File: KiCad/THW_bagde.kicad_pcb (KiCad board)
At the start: 2 copper layers, 84.9 x 84.9 mm, 19 parts, among them J1 USB_B, SW1 SW_Push, SW2 SW_Push, SW3 SW_Push, U1 ATmega32L-8P

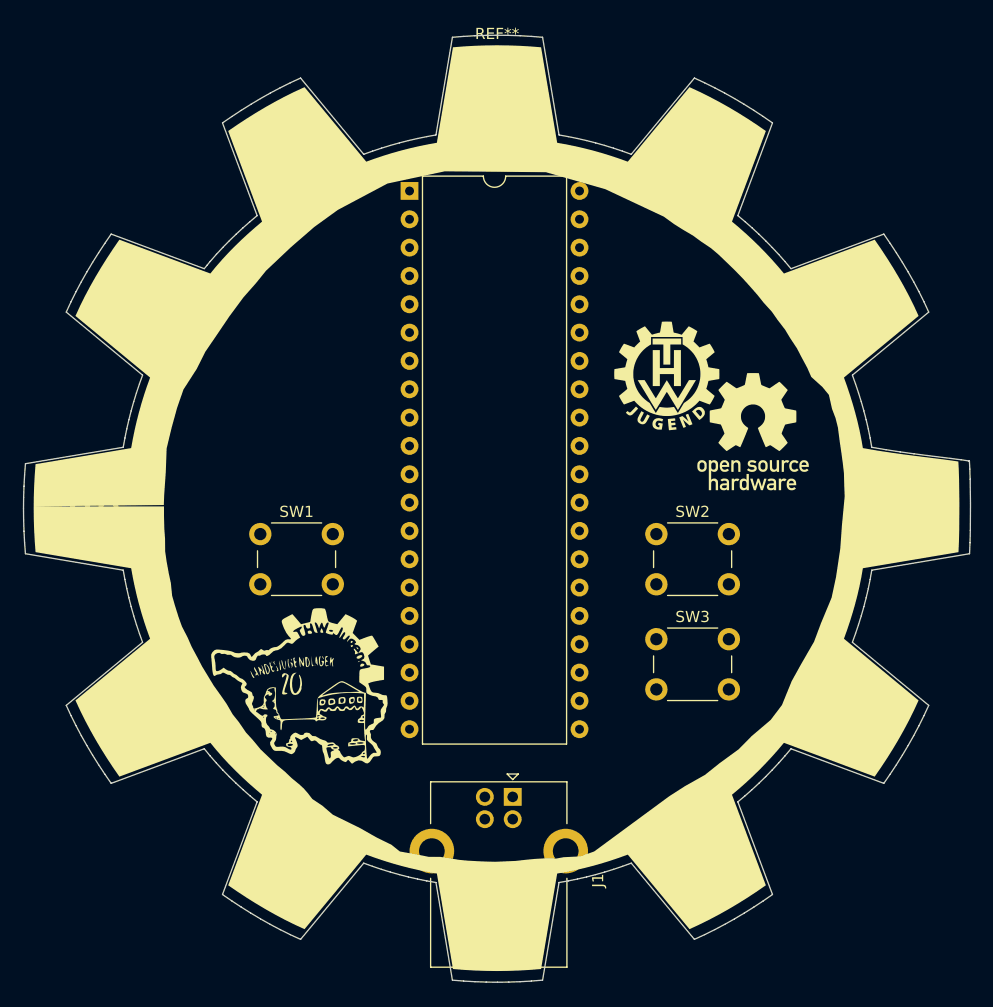
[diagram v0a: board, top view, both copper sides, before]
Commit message: place some parts to see dimension of badge
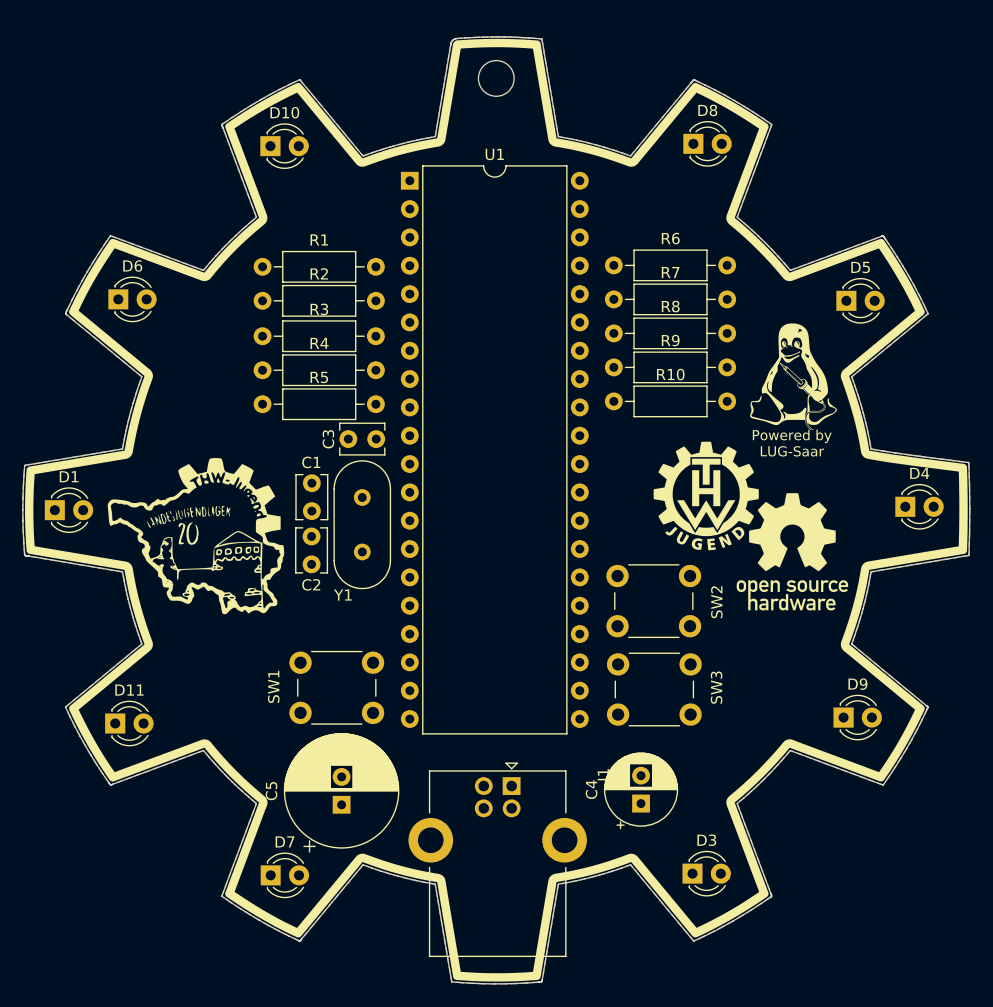
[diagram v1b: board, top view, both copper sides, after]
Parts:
- removed the REF** at (151.6, 53.9)
- added C1: C, Capacitor_THT:C_Disc_D3.8mm_W2.6mm_P2.50mm, F.Cu at (135.0, 92.5)
- added C2: C, Capacitor_THT:C_Disc_D3.8mm_W2.6mm_P2.50mm, F.Cu at (135.0, 97.3)
- added C3: C, Capacitor_THT:C_Disc_D3.8mm_W2.6mm_P2.50mm, F.Cu at (138.2, 86.1)
- added C4: C_Polarized, Capacitor_THT:CP_Radial_D6.3mm_P2.50mm, F.Cu at (164.5, 118.7)
- added C5: C_Polarized, Capacitor_THT:CP_Radial_D10.0mm_P2.50mm, F.Cu at (137.6, 118.8)
- added G***: LOGO, LOGO, F.Cu at (178.2, 78.8)
- added R1: R, Resistor_THT:R_Axial_DIN0207_L6.3mm_D2.5mm_P10.16mm_Horizontal, F.Cu at (130.6, 70.6)
- added R10: R, Resistor_THT:R_Axial_DIN0207_L6.3mm_D2.5mm_P10.16mm_Horizontal, F.Cu at (162.1, 82.7)
- added R2: R, Resistor_THT:R_Axial_DIN0207_L6.3mm_D2.5mm_P10.16mm_Horizontal, F.Cu at (130.6, 73.7)
- added R3: R, Resistor_THT:R_Axial_DIN0207_L6.3mm_D2.5mm_P10.16mm_Horizontal, F.Cu at (130.6, 76.8)
- added R4: R, Resistor_THT:R_Axial_DIN0207_L6.3mm_D2.5mm_P10.16mm_Horizontal, F.Cu at (130.6, 79.9)
- added R5: R, Resistor_THT:R_Axial_DIN0207_L6.3mm_D2.5mm_P10.16mm_Horizontal, F.Cu at (130.6, 82.9)
- added R6: R, Resistor_THT:R_Axial_DIN0207_L6.3mm_D2.5mm_P10.16mm_Horizontal, F.Cu at (162.1, 70.5)
- added R7: R, Resistor_THT:R_Axial_DIN0207_L6.3mm_D2.5mm_P10.16mm_Horizontal, F.Cu at (162.1, 73.5)
- added R8: R, Resistor_THT:R_Axial_DIN0207_L6.3mm_D2.5mm_P10.16mm_Horizontal, F.Cu at (162.1, 76.6)
- added R9: R, Resistor_THT:R_Axial_DIN0207_L6.3mm_D2.5mm_P10.16mm_Horizontal, F.Cu at (162.1, 79.6)
- added REF**: MountingHole_3.2mm_M3_DIN965, MountingHole:MountingHole_3.2mm_M3_DIN965, F.Cu at (151.5, 53.7)
- added Y1: Crystal, Crystal:Crystal_HC49-4H_Vertical, F.Cu at (139.5, 96.2)
- moved G*** 16.3 mm to (124.7, 93.9)
- moved SW1 12.1 mm to (134.0, 106.1)
- moved G*** 11.3 mm to (170.3, 91.2)
- moved G*** 11.3 mm to (178.1, 96.2)
- moved SW2 5.12 mm to (162.4, 98.3)
- moved SW3 4.11 mm to (162.4, 106.3)
- moved D1 2.27 mm to (111.9, 92.4)
- moved D11 1.71 mm to (117.3, 111.6)
- moved D3 1.60 mm to (169.1, 125.0)
- moved D10 1.53 mm to (131.3, 59.8)
- moved D8 1.50 mm to (169.2, 59.6)
- moved D6 1.49 mm to (117.6, 73.5)
- moved D7 1.34 mm to (131.3, 125.2)
- moved D4 1.29 mm to (188.2, 92.1)
- moved D9 1.29 mm to (182.6, 111.0)
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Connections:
- net Net-(U1-Pad11) renamed GND
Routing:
- added copper zone on B.Cu, net GND
- added copper zone on F.Cu, net GND
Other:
- outline, holes or cut-outs redrawn
- board text added: "Powered by LUG-Saar"

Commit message: adding lugsaar worksheet file
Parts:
- added D2: D, Diode_THT:D_DO-41_SOD81_P10.16mm_Horizontal, F.Cu at (133.3, 64.3)
- added R11: R, Resistor_THT:R_Axial_DIN0207_L6.3mm_D2.5mm_P10.16mm_Horizontal, F.Cu at (145.3, 98.9)
- added R12: R, Resistor_THT:R_Axial_DIN0207_L6.3mm_D2.5mm_P10.16mm_Horizontal, F.Cu at (143.5, 67.6)
- U1: value ATmega32L-8P -> ATmega328-P; footprint Package_DIP:DIP-40_W15.24mm -> Package_DIP:DIP-28_W7.62mm
- moved C5 15.2 mm to (147.7, 107.5), turned to -90 degrees
- moved C4 13.5 mm to (157.0, 107.5), turned to -90 degrees
- moved U1 6.72 mm to (148.0, 68.1)
- moved C2 5.01 mm to (136.4, 92.5)
- moved R1 2.79 mm to (133.3, 70.6)
- moved R2 2.79 mm to (133.3, 73.7)
- moved R3 2.79 mm to (133.3, 76.8)
- moved R4 2.79 mm to (133.3, 79.9)
- moved R5 2.79 mm to (133.3, 82.9)
- moved C3 2.77 mm to (141.0, 86.1)
- moved C1 2.61 mm to (136.4, 94.7), turned to -90 degrees
- moved Y1 1.47 mm to (141.0, 96.2)
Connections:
- C1 pad 1: unconnected-(C1-Pad1) -> Net-(U1-Pad10)
- C1 pad 2: unconnected-(C1-Pad2) -> GND
- C2 pad 1: unconnected-(C2-Pad1) -> Net-(U1-Pad9)
- C2 pad 2: unconnected-(C2-Pad2) -> GND
- C3 pad 1: unconnected-(C3-Pad1) -> +5V
- C3 pad 2: unconnected-(C3-Pad2) -> GND
- J1 pad 4: unconnected-(J1-Pad4) -> GND
- J1 pad 5: unconnected-(J1-Pad5) -> GND
- SW1 pad 1: unconnected-(SW1-Pad1) -> Net-(U1-Pad1)
- SW1 pad 2: unconnected-(SW1-Pad2) -> GND
- U1 pad 1: unconnected-(U1-Pad1) -> Net-(U1-Pad1)
- U1 pad 10: unconnected-(U1-Pad10) -> Net-(U1-Pad10)
- U1 pad 11: GND -> unconnected-(U1-Pad11)
- U1 pad 20: unconnected-(U1-Pad20) -> +5V
- U1 pad 22: unconnected-(U1-Pad22) -> GND
- U1 pad 7: unconnected-(U1-Pad7) -> +5V
- U1 pad 8: unconnected-(U1-Pad8) -> GND
- U1 pad 9: unconnected-(U1-Pad9) -> Net-(U1-Pad9)
- Y1 pad 1: unconnected-(Y1-Pad1) -> Net-(U1-Pad10)
- Y1 pad 2: unconnected-(Y1-Pad2) -> Net-(U1-Pad9)

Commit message: LED placement
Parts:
- C5: footprint Capacitor_THT:CP_Radial_D10.0mm_P2.50mm -> Capacitor_THT:CP_Radial_D6.3mm_P2.50mm
- moved D4 74.0 mm to (116.8, 111.8)
- moved D6 72.3 mm to (168.9, 124.5)
- moved D5 71.9 mm to (132.1, 124.5)
- moved D3 64.7 mm to (113.0, 92.7)
- moved D7 53.4 mm to (182.6, 110.5)
- moved D1 38.4 mm to (132.1, 59.7)
- moved D2 38.4 mm to (117.3, 73.2)
- moved D10 37.6 mm to (168.9, 59.9)
- moved D8 37.6 mm to (188.0, 92.2)
- moved D9 37.1 mm to (182.6, 73.9)
- moved R6 27.8 mm to (160.5, 82.8)
- moved R8 27.3 mm to (160.5, 75.7)
- moved R7 27.2 mm to (160.5, 79.2)
- moved R5 19.9 mm to (143.5, 83.8), turned to 180 degrees
- moved R3 18.9 mm to (143.5, 77.2), turned to 180 degrees
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- renumbered D2 to D11, D11 to D2, R9 to R10, R5 to R2, R7 to R3, R10 to R4, R8 to R5, R3 to R6, R4 to R7, R2 to R8, R6 to R9
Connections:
- D1 pad 1: unconnected-(D1-Pad1) -> GND
- D1 pad 2: unconnected-(D1-Pad2) -> Net-(D1-Pad2)
- D10 pad 1: unconnected-(D10-Pad1) -> GND
- D10 pad 2: unconnected-(D10-Pad2) -> Net-(R10-Pad2)
- D2 pad 1: unconnected-(D11-Pad1) -> GND
- D2 pad 2: unconnected-(D11-Pad2) -> Net-(D2-Pad2)
- D3 pad 1: unconnected-(D3-Pad1) -> GND
- D3 pad 2: unconnected-(D3-Pad2) -> Net-(D3-Pad2)
- D4 pad 1: unconnected-(D4-Pad1) -> GND
- D4 pad 2: unconnected-(D4-Pad2) -> Net-(D4-Pad2)
- D5 pad 1: unconnected-(D5-Pad1) -> GND
- D5 pad 2: unconnected-(D5-Pad2) -> Net-(D5-Pad2)
- D6 pad 1: unconnected-(D6-Pad1) -> GND
- D6 pad 2: unconnected-(D6-Pad2) -> Net-(R6-Pad2)
- D7 pad 1: unconnected-(D7-Pad1) -> GND
- D7 pad 2: unconnected-(D7-Pad2) -> Net-(R7-Pad2)
- D8 pad 1: unconnected-(D8-Pad1) -> GND
- D8 pad 2: unconnected-(D8-Pad2) -> Net-(R8-Pad2)
- D9 pad 1: unconnected-(D9-Pad1) -> GND
- D9 pad 2: unconnected-(D9-Pad2) -> Net-(R9-Pad2)
- R1 pad 1: unconnected-(R1-Pad1) -> /PD0
- R1 pad 2: unconnected-(R1-Pad2) -> Net-(D1-Pad2)
- R10 pad 1: unconnected-(R9-Pad1) -> /PC5
- R10 pad 2: unconnected-(R9-Pad2) -> Net-(R10-Pad2)
- R2 pad 1: unconnected-(R5-Pad1) -> /PD1
- R2 pad 2: unconnected-(R5-Pad2) -> Net-(D2-Pad2)
- R3 pad 1: unconnected-(R7-Pad1) -> /PD2
- R3 pad 2: unconnected-(R7-Pad2) -> Net-(D3-Pad2)
- R4 pad 1: unconnected-(R10-Pad1) -> /PD3
- R4 pad 2: unconnected-(R10-Pad2) -> Net-(D4-Pad2)
- R5 pad 1: unconnected-(R8-Pad1) -> /PD4
- R5 pad 2: unconnected-(R8-Pad2) -> Net-(D5-Pad2)
- R6 pad 1: unconnected-(R3-Pad1) -> /PC1
- R6 pad 2: unconnected-(R3-Pad2) -> Net-(R6-Pad2)
- R7 pad 1: unconnected-(R4-Pad1) -> /PC2
- R7 pad 2: unconnected-(R4-Pad2) -> Net-(R7-Pad2)
- R8 pad 1: unconnected-(R2-Pad1) -> /PC3
- R8 pad 2: unconnected-(R2-Pad2) -> Net-(R8-Pad2)
- R9 pad 1: unconnected-(R6-Pad1) -> /PC4
- R9 pad 2: unconnected-(R6-Pad2) -> Net-(R9-Pad2)
- U1 pad 2: unconnected-(U1-Pad2) -> /PD0
- U1 pad 24: unconnected-(U1-Pad24) -> /PC1
- U1 pad 25: unconnected-(U1-Pad25) -> /PC2
- U1 pad 26: unconnected-(U1-Pad26) -> /PC3
- U1 pad 27: unconnected-(U1-Pad27) -> /PC4
- U1 pad 28: unconnected-(U1-Pad28) -> /PC5
- U1 pad 3: unconnected-(U1-Pad3) -> /PD1
- U1 pad 4: unconnected-(U1-Pad4) -> /PD2
- U1 pad 5: unconnected-(U1-Pad5) -> /PD3
- U1 pad 6: unconnected-(U1-Pad6) -> /PD4

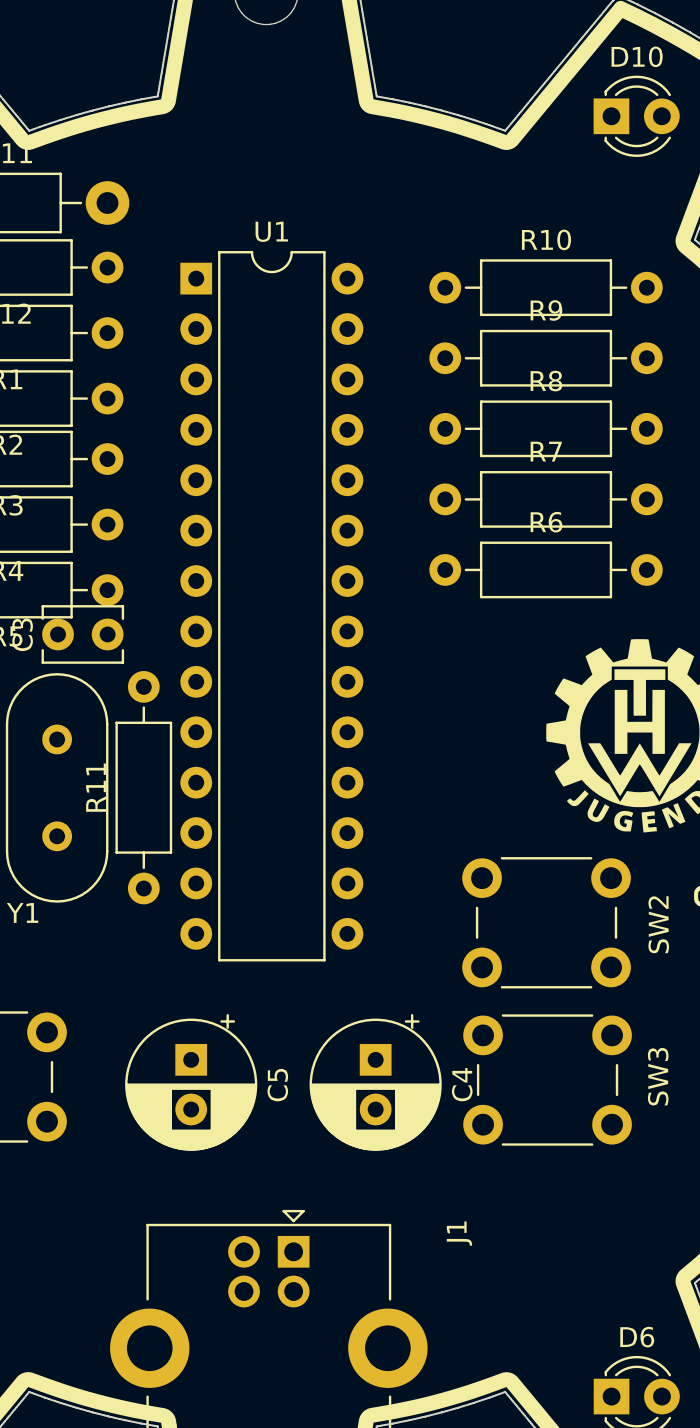
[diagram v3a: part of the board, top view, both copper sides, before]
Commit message: ICSP-Header added
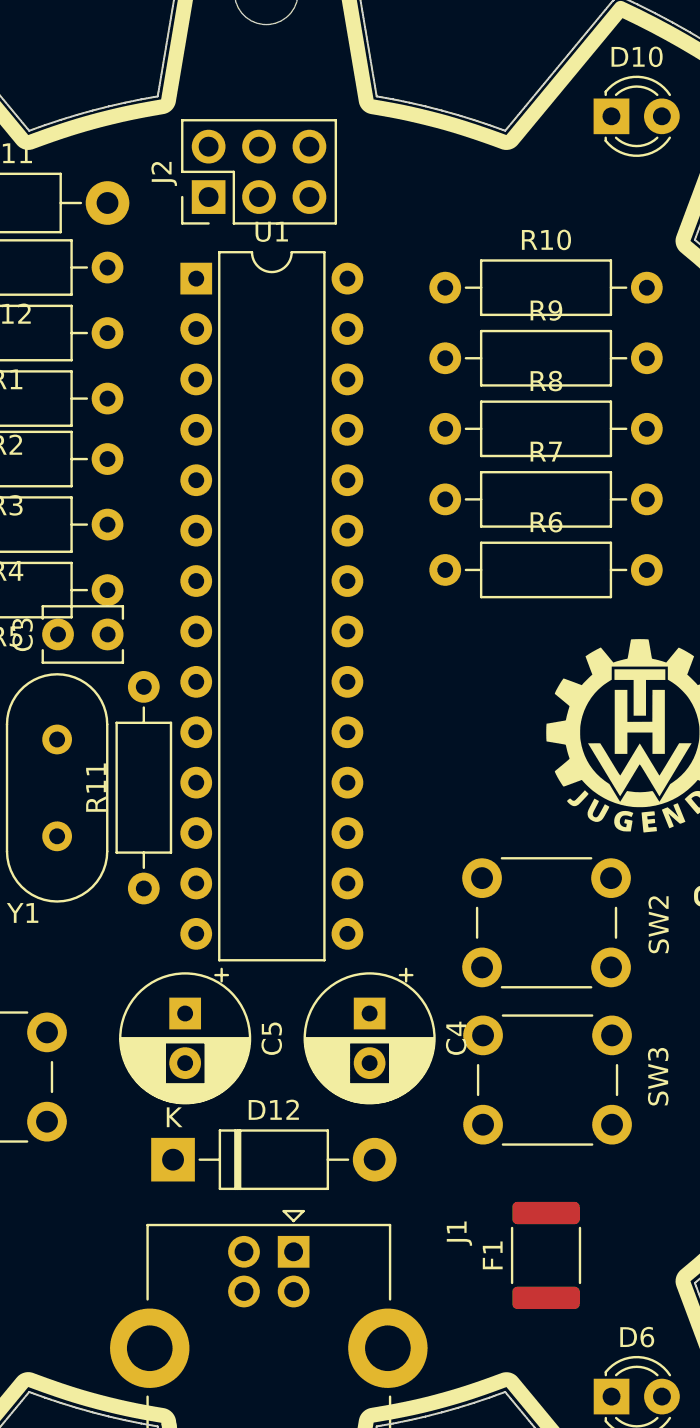
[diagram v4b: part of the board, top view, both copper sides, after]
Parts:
- added D12: D, Diode_THT:D_DO-41_SOD81_P10.16mm_Horizontal, F.Cu at (146.8, 112.5)
- added F1: MF-MSMF050-2, Fuse:Fuse_1812_4532Metric, F.Cu at (165.6, 117.3)
- added J2: Conn_02x03_Odd_Even, Connector_PinHeader_2.54mm:PinHeader_2x03_P2.54mm_Vertical, F.Cu at (148.6, 64.0)
- moved C4 2.36 mm to (156.7, 105.2)
- moved C5 2.36 mm to (147.4, 105.2)
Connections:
- net Net-(D11-Pad2) renamed /RES
- C4 pad 1: unconnected-(C4-Pad1) -> +5V
- C4 pad 2: unconnected-(C4-Pad2) -> GND
- C5 pad 1: unconnected-(C5-Pad1) -> +5V
- C5 pad 2: unconnected-(C5-Pad2) -> GND
- J1 pad 1: unconnected-(J1-Pad1) -> Net-(J1-Pad1)
- U1 pad 17: unconnected-(U1-Pad17) -> /MOSI
- U1 pad 18: unconnected-(U1-Pad18) -> /MISO
- U1 pad 19: unconnected-(U1-Pad19) -> /SCK

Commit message: adding firmware for tests
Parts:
- added C6: C, Capacitor_THT:C_Disc_D3.8mm_W2.6mm_P2.50mm, F.Cu at (141.1, 105.8)
- added C7: C, Capacitor_THT:C_Disc_D3.8mm_W2.6mm_P2.50mm, F.Cu at (161.8, 105.8)
- added R13: 10k, Resistor_THT:R_Axial_DIN0207_L6.3mm_D2.5mm_P10.16mm_Horizontal, F.Cu at (163.4, 112.6)
- added R14: 10k, Resistor_THT:R_Axial_DIN0207_L6.3mm_D2.5mm_P10.16mm_Horizontal, F.Cu at (129.6, 112.6)
- J2: value Conn_02x03_Odd_Even -> ISP
- R12: value R -> 10k
- moved SW1 35.5 mm to (161.4, 83.6)
- moved SW2 31.8 mm to (131.3, 104.9)
- moved F1 8.79 mm to (158.2, 112.6), turned to 180 degrees
- moved G*** 4.59 mm to (168.9, 95.5)
- moved G*** 4.49 mm to (177.1, 83.2)
- moved D12 3.25 mm to (143.6, 112.6)
- moved SW3 3.04 mm to (165.2, 104.9)
- moved R6 2.69 mm to (159.5, 80.3)
- moved R7 2.23 mm to (159.5, 77.3)
- moved G*** 1.95 mm to (177.8, 98.1)
- moved C1 1.92 mm to (135.1, 96.1)
- moved C2 1.92 mm to (135.1, 93.9)
- moved R11 1.92 mm to (144.0, 100.3)
- moved Y1 1.92 mm to (139.7, 97.6)
- moved R8 1.79 mm to (159.5, 74.2)
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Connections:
- SW2 pad 1: unconnected-(SW2-Pad1) -> +5V
- SW2 pad 2: unconnected-(SW2-Pad2) -> Net-(SW2-Pad2)
- SW3 pad 1: unconnected-(SW3-Pad1) -> +5V
- SW3 pad 2: unconnected-(SW3-Pad2) -> Net-(SW3-Pad2)
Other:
- board size 84.9 x 84.9 mm -> 84.9 x 82.9 mm

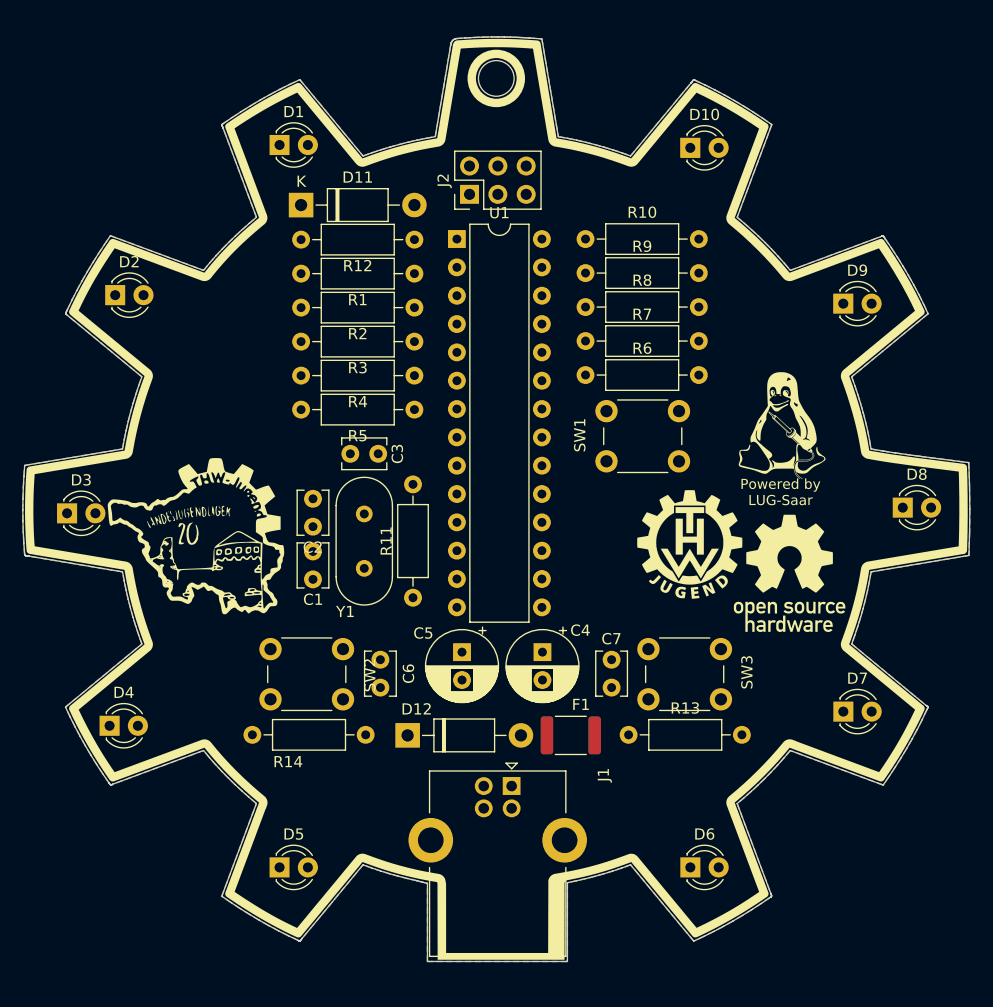
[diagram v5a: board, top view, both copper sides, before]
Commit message: fixing some silkscreen issues and adding image to README file
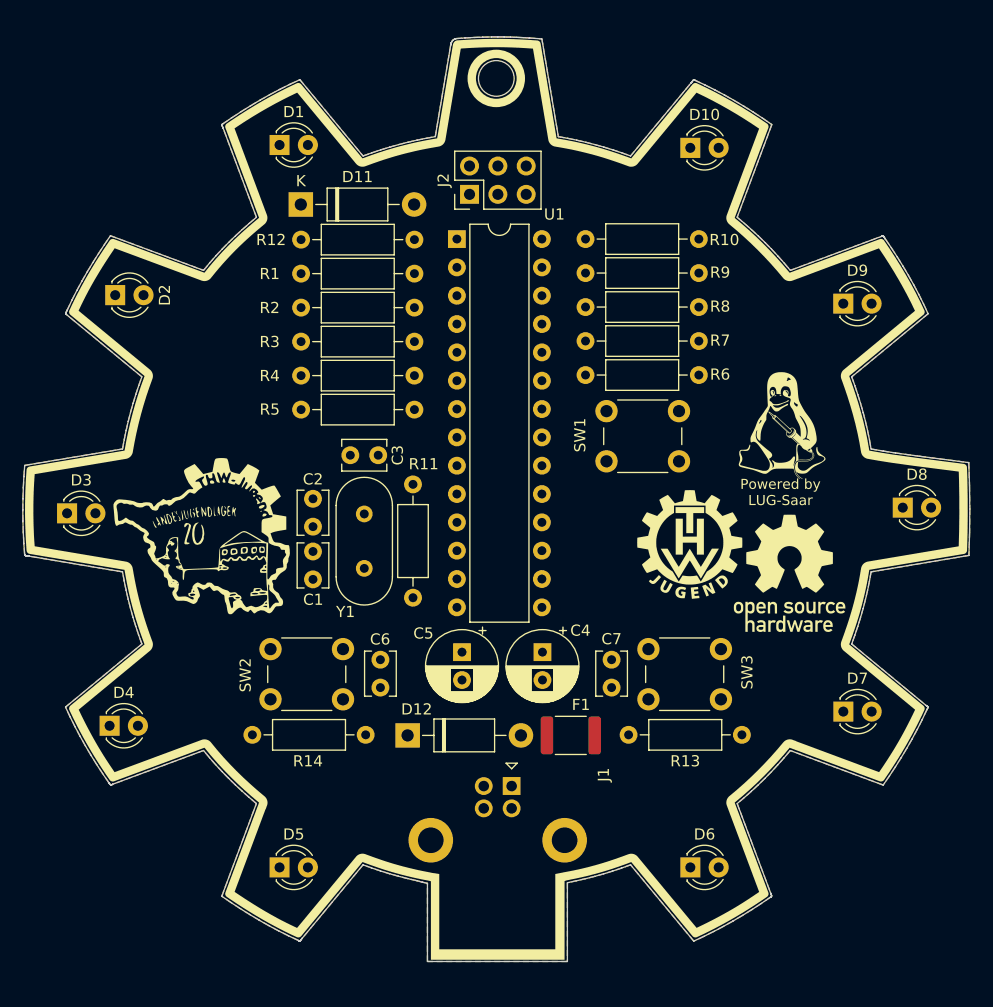
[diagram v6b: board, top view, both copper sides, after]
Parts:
- moved G*** 0.51 mm to (125.2, 93.9)
- moved C3 0.13 mm to (140.9, 87.5)
- moved D11 0.06 mm to (134.0, 65.0)
